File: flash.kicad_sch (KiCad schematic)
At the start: 2 parts, among them U2 W25Q128JVSIQ

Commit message: WIP
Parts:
- U2: value W25Q128JVSIQ -> SST26VF016BEUI-104I/SN; footprint Package_SO:SOIC-8_5.23x5.23mm_P1.27mm -> Package_SO:SOIC-8_3.9x4.9mm_P1.27mm; symbol Memory_Flash:W25Q32JVSS -> Project_Library:Microchip Technology SST26VF016BEUI-104I/SN; JLCPCB Part # (none) -> C631791; Manufacturer (none) -> Microchip Tech; Partnumber (none) -> SST26VF016BEUI-104I/SN; isBasicPart (none) -> NO; now fitted; now in the parts list
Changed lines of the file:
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@@
     (effects (font (size 1 1)) (justify right))
   )
-  (symbol (lib_id "Memory_Flash:W25Q32JVSS") (at 71.755 34.925 0) (unit 1)
-    (in_bom no) (on_board yes) (dnp yes) (fields_autoplaced)
-    (property "Reference" "U2" (at 80.645 33.655 0)
+  (symbol (lib_id "Project_Library:Microchip Technology SST26VF016BEUI-104I/SN") (at 71.755 34.925 0) (unit 1)
+    (in_bom yes) (on_board yes) (dnp no) (fields_autoplaced)
+    (property "Reference" "U2" (at 81.28 33.6549 0)
       (effects (font (size 1 1)) (justify left))
     )
-    (property "Value" "W25Q128JVSIQ" (at 80.645 36.195 0)
+    (property "Value" "SST26VF016BEUI-104I/SN" (at 81.28 36.1949 0)
       (effects (font (size 1 1)) (justify left))
     )
-    (property "Footprint" "Package_SO:SOIC-8_5.23x5.23mm_P1.27mm" (at 71.755 34.925 0)
-      (effects (font (size 1 1)) hide)
+    (property "Footprint" "Package_SO:SOIC-8_3.9x4.9mm_P1.27mm" (at 71.755 52.705 0)
+      (effects (font (size 1.27 1.27)) hide)
     )
-    (property "Datasheet" "http://www.winbond.com/resource-files/w25q32jv%20revg%2003272018%20plus.pdf" (at 71.755 34.925 0)
-      (effects (font (size 1 1)) hide)
+    (property "Datasheet" "http://ww1.microchip.com/downloads/en/DeviceDoc/20005045C.pdf" (at 71.755 57.785 0)
+      (effects (font (size 1.27 1.27)) hide)
     )
-    (property "Description" "SOP-8-208mil NOR FLASH ROHS" (at 71.755 34.925 0)
-      (effects (font (size 1 1)) hide)
+    (property "Description" "NOR-Flash 16Mbit SPI/SQI Flash w/EUI, 85C, 2.3V-3.6V" (at 71.755 62.865 0)
+      (effects (font (size 1.27 1.27)) hide)
     )
-    (property "Manufacturer" "Winbond Elec" (at 71.755 34.925 0)
-      (effects (font (size 1 1)) hide)
+    (property "Manufacturer" "Microchip Tech" (at 71.755 65.405 0)
+      (effects (font (size 1.27 1.27)) hide)
     )
-    (property "Partnumber" "W25Q128JVSIQ" (at 71.755 34.925 0)
-      (effects (font (size 1 1)) hide)
+    (property "Partnumber" "SST26VF016BEUI-104I/SN" (at 71.755 60.325 0)
+      (effects (font (size 1.27 1.27)) hide)
     )
-    (property "JLCPCB Part #" "C97521" (at 71.755 34.925 0)
-      (effects (font (size 1 1)) hide)
+    (property "JLCPCB Part #" "C631791" (at 71.755 55.245 0) (show_name)
+      (effects (font (size 1.27 1.27)) hide)
     )
-    (property "isBasicPart" "YES" (at 71.755 34.925 0)
-      (effects (font (size 1 1)) hide)
+    (property "isBasicPart" "NO" (at 71.755 67.945 0) (show_name)
+      (effects (font (size 1.27 1.27)) hide)
     )
-    (property "Description" "" (at 71.755 34.925 0)
-      (effects (font (size 1 1)) hide)
+    (property "Description" "NOR-Flash 16Mbit SPI/SQI Flash w/EUI, 85C, 2.3V-3.6V" (at 71.755 62.865 0)
+      (effects (font (size 1.27 1.27)) hide)
     )
-    (property "Manufacturer" "" (at 71.755 34.925 0)
-      (effects (font (size 1 1)) hide)
+    (property "Manufacturer" "Microchip Tech" (at 71.755 65.405 0)
+      (effects (font (size 1.27 1.27)) hide)
     )
-    (property "Partnumber" "" (at 71.755 34.925 0)
-      (effects (font (size 1 1)) hide)
+    (property "Partnumber" "SST26VF016BEUI-104I/SN" (at 71.755 60.325 0)
+      (effects (font (size 1.27 1.27)) hide)
     )
-    (property "JLCPCB Part #" "" (at 71.755 34.925 0)
-      (effects (font (size 1 1)) hide)
+    (property "JLCPCB Part #" "C631791" (at 71.755 55.245 0) (show_name)
+      (effects (font (size 1.27 1.27)) hide)
     )
-    (property "isBasicPart" "" (at 71.755 34.925 0)
-      (effects (font (size 1 1)) hide)
+    (property "isBasicPart" "NO" (at 71.755 67.945 0) (show_name)
+      (effects (font (size 1.27 1.27)) hide)
     )
     (pin "1")

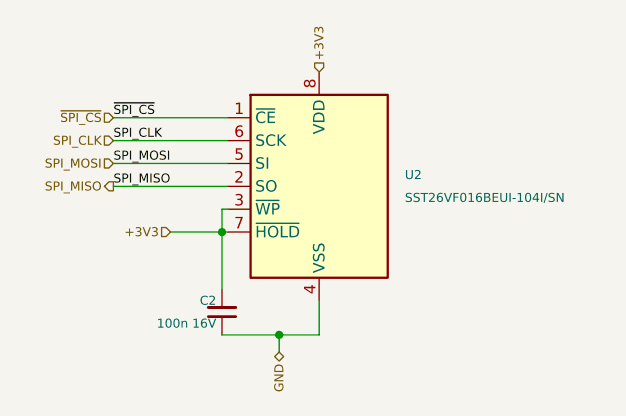
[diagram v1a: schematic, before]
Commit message: Set DNP on devices not to populate
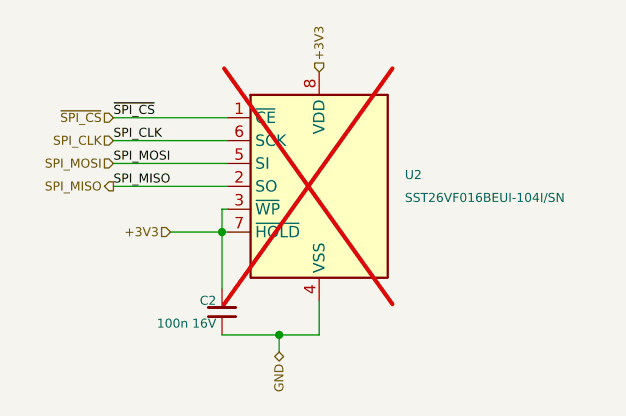
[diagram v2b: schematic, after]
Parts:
- U2: now not fitted; now left out of the parts list
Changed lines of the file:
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@@
   )
   (symbol (lib_id "Project_Library:Microchip Technology SST26VF016BEUI-104I/SN") (at 71.755 34.925 0) (unit 1)
-    (in_bom yes) (on_board yes) (dnp no) (fields_autoplaced)
+    (in_bom no) (on_board yes) (dnp yes) (fields_autoplaced)
     (property "Reference" "U2" (at 81.28 33.6549 0)
       (effects (font (size 1 1)) (justify left))

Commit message: #1 Use new central library KiCad-Lib
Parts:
- U2: symbol Project_Library:Microchip Technology SST26VF016BEUI-104I/SN -> #IC:Microchip Technology SST26VF016BEUI-104I/SN; now in the parts list
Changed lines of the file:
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@@
     (effects (font (size 1 1)) (justify right))
   )
-  (symbol (lib_id "Project_Library:Microchip Technology SST26VF016BEUI-104I/SN") (at 71.755 34.925 0) (unit 1)
-    (in_bom no) (on_board yes) (dnp yes) (fields_autoplaced)
+  (symbol (lib_id "#IC:Microchip Technology SST26VF016BEUI-104I/SN") (at 71.755 34.925 0) (unit 1)
+    (in_bom yes) (on_board yes) (dnp yes) (fields_autoplaced)
     (property "Reference" "U2" (at 81.28 33.6549 0)
       (effects (font (size 1 1)) (justify left))
@@
       (effects (font (size 1.27 1.27)) hide)
     )
-    (property "Datasheet" "http://ww1.microchip.com/downloads/en/DeviceDoc/20005045C.pdf" (at 71.755 57.785 0)
+    (property "Datasheet" "${KIPRJMOD}/KiCad-Lib/#IC.doc/Microchip Technology SST26VF016BEUI-104ISN.pdf" (at 71.755 57.785 0)
       (effects (font (size 1.27 1.27)) hide)
     )

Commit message: WIP
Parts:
- U2: now fitted; now left out of the parts list
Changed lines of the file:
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@@
   )
   (symbol (lib_id "#IC:Microchip Technology SST26VF016BEUI-104I/SN") (at 71.755 34.925 0) (unit 1)
-    (in_bom yes) (on_board yes) (dnp yes) (fields_autoplaced)
+    (in_bom no) (on_board yes) (dnp no) (fields_autoplaced)
     (property "Reference" "U2" (at 81.28 33.6549 0)
       (effects (font (size 1 1)) (justify left))
@@
         )
         (path "/e63e39d7-6ac0-4ffd-8aa3-1841a4541b55/0d09f1c5-80ef-4ecd-bc99-7e5b757caf07"
-          (reference "U501") (unit 1)
+          (reference "U301") (unit 1)
         )
       )
@@
       (project "stm32f4_uno"
         (path "/e63e39d7-6ac0-4ffd-8aa3-1841a4541b55/0d09f1c5-80ef-4ecd-bc99-7e5b757caf07"
-          (reference "C501") (unit 1)
+          (reference "C301") (unit 1)
         )
       )

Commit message: #2 Add silkscreen texts
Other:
- company: (none) -> easy-smart solution GmbH
- title: (none) -> STM32F4 Uno
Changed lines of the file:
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@@
 (kicad_sch (version 20230121) (generator eeschema)
   (paper "A4")
+  (title_block
+    (title "STM32F4 Uno")
+    (date "2023-10-02")
+    (rev "1.0.x-dev")
+    (company "easy-smart solution GmbH")
+  )
   (junction (at 67.31 51.435) (diameter 0) (color 0 0 0 0)
   )
